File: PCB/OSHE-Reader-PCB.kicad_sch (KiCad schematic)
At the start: 1 part

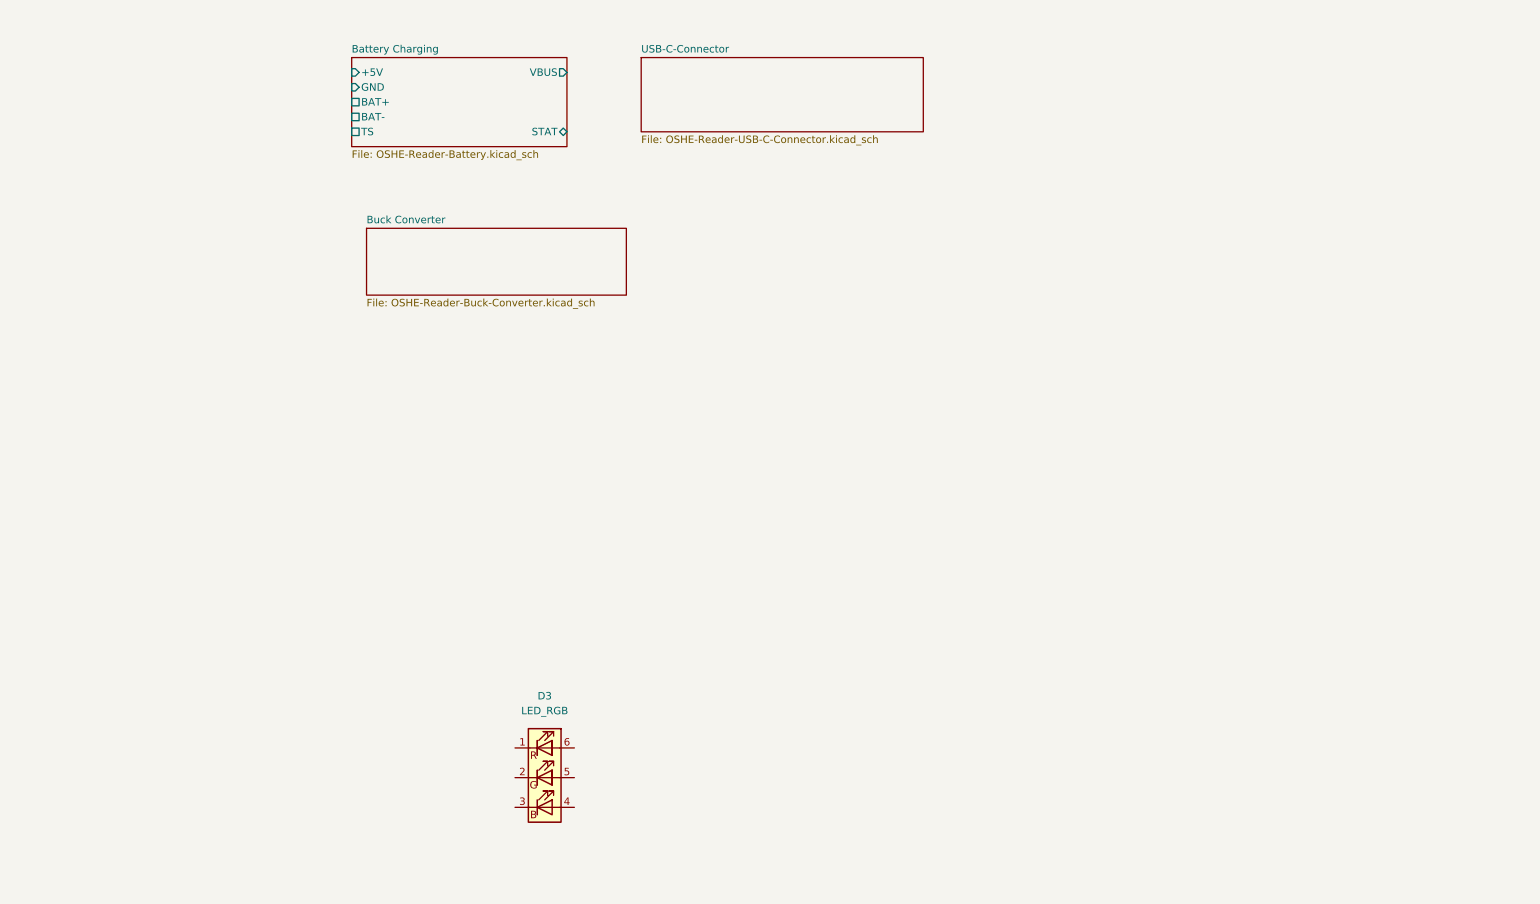
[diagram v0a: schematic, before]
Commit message: added hierarchical symbols to Buck, and did miscelaneous fixes
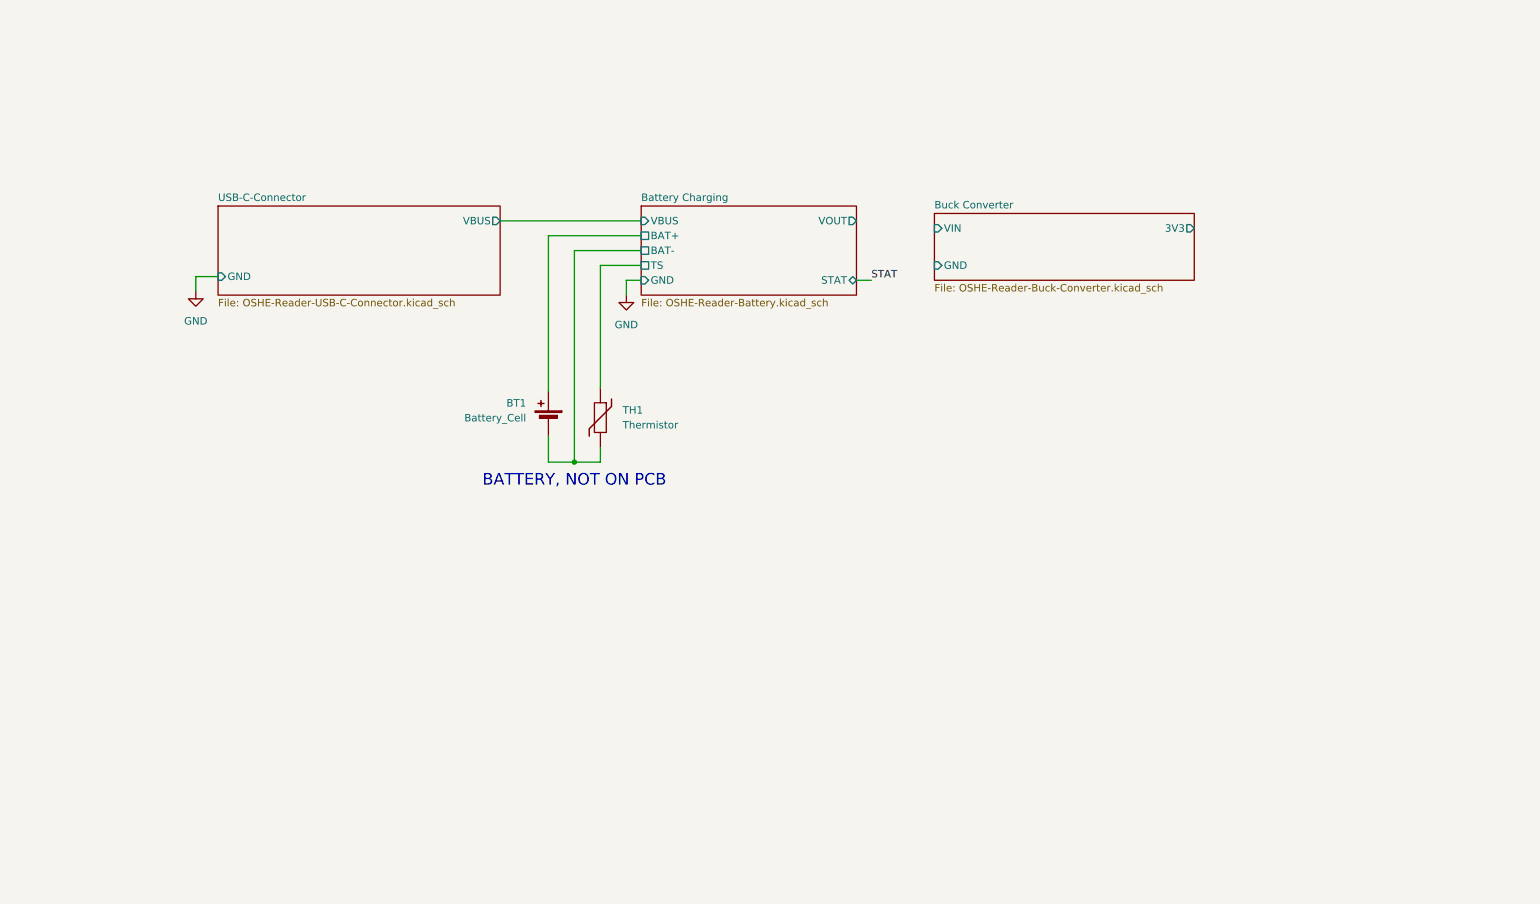
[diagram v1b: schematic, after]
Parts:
- removed D3: LED_RGB, symbol Device:LED_RGB
- added BT1: Battery_Cell, symbol Device:Battery_Cell
- added TH1: Thermistor, symbol Device:Thermistor
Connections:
- net Battery Charging/BAT+: now also BT1.1 (+)
- net Battery Charging/BAT-: now also BT1.2 (-), TH1.2
- net Battery Charging/TS: now also TH1.1
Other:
- sheet Battery Charging ports: added VOUT; removed +5V
- sheet Buck Converter ports: added 3V3, GND, VIN; removed none
- sheet USB-C-Connector ports: added GND, VBUS; removed none
- note added: "BATTERY, NOT ON PCB"

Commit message: fixed up the pcb so everything is *basically* passing ERC
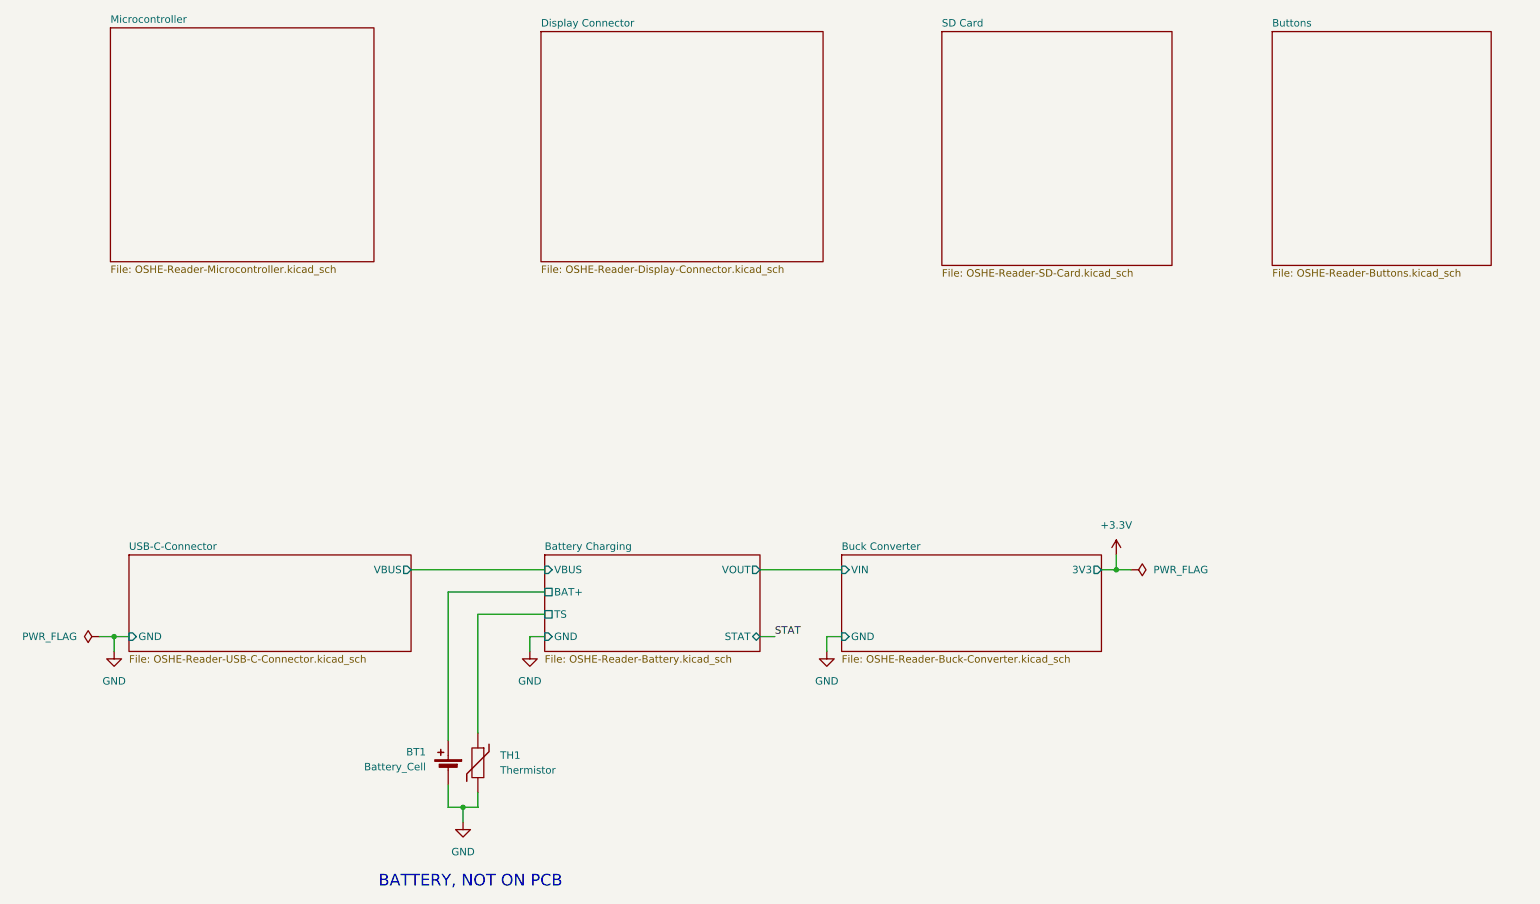
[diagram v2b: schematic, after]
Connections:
- net Battery Charging/BAT- is gone; now on net GND: BT1.2 (-), TH1.2
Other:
- added sheet Buttons (OSHE-Reader-Buttons.kicad_sch)
- added sheet Display Connector (OSHE-Reader-Display-Connector.kicad_sch)
- added sheet Microcontroller (OSHE-Reader-Microcontroller.kicad_sch)
- added sheet SD Card (OSHE-Reader-SD-Card.kicad_sch)
- sheet Battery Charging ports: added none; removed BAT-
- moved on the sheet: BT1, TH1

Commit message: started work adding hierarchical power pins to mcu and sd card sheets
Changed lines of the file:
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@@
 	)
 	(junction
-		(at 201.93 125.73)
+		(at 204.47 125.73)
 		(diameter 0)
 		(color 0 0 0 0)
@@
 	(wire
 		(pts
-			(xy 201.93 123.19) (xy 201.93 125.73)
+			(xy 204.47 123.19) (xy 204.47 125.73)
+		)
+		(stroke
+			(width 0)
+			(type default)
+		)
+	)
+	(wire
+		(pts
+			(xy 204.47 125.73) (xy 207.01 125.73)
+		)
+		(stroke
+			(width 0)
+			(type default)
+		)
+	)
+	(wire
+		(pts
+			(xy 140.97 125.73) (xy 157.48 125.73)
+		)
+		(stroke
+			(width 0)
+			(type default)
+		)
+	)
+	(wire
+		(pts
+			(xy 87.63 166.37) (xy 87.63 162.56)
+		)
+		(stroke
+			(width 0)
+			(type default)
+		)
+	)
+	(wire
+		(pts
+			(xy 90.17 166.37) (xy 90.17 168.91)
+		)
+		(stroke
+			(width 0)
+			(type default)
+		)
+	)
+	(wire
+		(pts
+			(xy 87.63 154.94) (xy 87.63 129.54)
+		)
+		(stroke
+			(width 0)
+			(type default)
+		)
+	)
+	(wire
+		(pts
+			(xy 30.48 137.16) (xy 33.02 137.16)
+		)
+		(stroke
+			(width 0)
+			(type default)
+		)
+	)
+	(wire
+		(pts
+			(xy 30.48 137.16) (xy 30.48 139.7)
+		)
+		(stroke
+			(width 0)
+			(type default)
+		)
+	)
+	(wire
+		(pts
+			(xy 81.28 125.73) (xy 104.14 125.73)
+		)
+		(stroke
+			(width 0)
+			(type default)
+		)
+	)
+	(wire
+		(pts
+			(xy 92.71 133.35) (xy 104.14 133.35)
+		)
+		(stroke
+			(width 0)
+			(type default)
+		)
+	)
+	(wire
+		(pts
+			(xy 90.17 166.37) (xy 92.71 166.37)
 		)
 		(stroke
@@
 	(wire
 		(pts
-			(xy 140.97 125.73) (xy 154.94 125.73)
-		)
-		(stroke
-			(width 0)
-			(type default)
-		)
-	)
-	(wire
-		(pts
-			(xy 87.63 166.37) (xy 87.63 162.56)
-		)
-		(stroke
-			(width 0)
-			(type default)
-		)
-	)
-	(wire
-		(pts
-			(xy 90.17 166.37) (xy 90.17 168.91)
-		)
-		(stroke
-			(width 0)
-			(type default)
-		)
-	)
-	(wire
-		(pts
-			(xy 87.63 154.94) (xy 87.63 129.54)
-		)
-		(stroke
-			(width 0)
-			(type default)
-		)
-	)
-	(wire
-		(pts
-			(xy 30.48 137.16) (xy 33.02 137.16)
-		)
-		(stroke
-			(width 0)
-			(type default)
-		)
-	)
-	(wire
-		(pts
-			(xy 30.48 137.16) (xy 30.48 139.7)
-		)
-		(stroke
-			(width 0)
-			(type default)
-		)
-	)
-	(wire
-		(pts
-			(xy 81.28 125.73) (xy 104.14 125.73)
-		)
-		(stroke
-			(width 0)
-			(type default)
-		)
-	)
-	(wire
-		(pts
-			(xy 92.71 133.35) (xy 104.14 133.35)
-		)
-		(stroke
-			(width 0)
-			(type default)
-		)
-	)
-	(wire
-		(pts
-			(xy 90.17 166.37) (xy 92.71 166.37)
-		)
-		(stroke
-			(width 0)
-			(type default)
-		)
-	)
-	(wire
-		(pts
-			(xy 199.39 125.73) (xy 201.93 125.73)
-		)
-		(stroke
-			(width 0)
-			(type default)
-		)
-	)
-	(wire
-		(pts
 			(xy 92.71 153.67) (xy 92.71 133.35)
 		)
@@
 	(wire
 		(pts
-			(xy 152.4 137.16) (xy 152.4 139.7)
+			(xy 154.94 137.16) (xy 154.94 139.7)
 		)
 		(stroke
@@
 	(wire
 		(pts
-			(xy 152.4 137.16) (xy 154.94 137.16)
-		)
-		(stroke
-			(width 0)
-			(type default)
-		)
-	)
-	(label "STAT"
+			(xy 154.94 137.16) (xy 157.48 137.16)
+		)
+		(stroke
+			(width 0)
+			(type default)
+		)
+	)
+	(label "BAT_STAT"
 		(at 143.51 137.16 0)
 		(effects
@@
 	(symbol
 		(lib_id "power:GND")
-		(at 152.4 139.7 0)
+		(at 154.94 139.7 0)
 		(unit 1)
 		(exclude_from_sim no)
@@
 		(fields_autoplaced yes)
 		(property "Reference" "#PWR03"
-			(at 152.4 146.05 0)
+			(at 154.94 146.05 0)
 			(effects
 				(font
@@
 		)
 		(property "Value" "GND"
-			(at 152.4 144.78 0)
+			(at 154.94 144.78 0)
 			(effects
 				(font
@@
 		)
 		(property "Footprint" ""
-			(at 152.4 139.7 0)
+			(at 154.94 139.7 0)
 			(effects
 				(font
@@
 		)
 		(property "Datasheet" ""
-			(at 152.4 139.7 0)
+			(at 154.94 139.7 0)
 			(effects
 				(font
@@
 		)
 		(property "Description" "Power symbol creates a global label with name \"GND\" , ground"
-			(at 152.4 139.7 0)
+			(at 154.94 139.7 0)
 			(effects
 				(font
@@
 	(symbol
 		(lib_id "power:PWR_FLAG")
-		(at 204.47 125.73 270)
+		(at 207.01 125.73 270)
 		(unit 1)
 		(exclude_from_sim no)
@@
 		(fields_autoplaced yes)
 		(property "Reference" "#FLG02"
-			(at 206.375 125.73 0)
+			(at 208.915 125.73 0)
 			(effects
 				(font
@@
 		)
 		(property "Value" "PWR_FLAG"
-			(at 208.28 125.7299 90)
+			(at 210.82 125.7299 90)
 			(effects
 				(font
@@
 		)
 		(property "Footprint" ""
-			(at 204.47 125.73 0)
+			(at 207.01 125.73 0)
 			(effects
 				(font
@@
 		)
 		(property "Datasheet" "~"
-			(at 204.47 125.73 0)
+			(at 207.01 125.73 0)
 			(effects
 				(font
@@
 		)
 		(property "Description" "Special symbol for telling ERC where power comes from"
-			(at 204.47 125.73 0)
+			(at 207.01 125.73 0)
 			(effects
 				(font
@@
 	(symbol
 		(lib_id "power:+3.3V")
-		(at 201.93 123.19 0)
+		(at 204.47 123.19 0)
 		(unit 1)
 		(exclude_from_sim no)
@@
 		(fields_autoplaced yes)
 		(property "Reference" "#PWR04"
-			(at 201.93 127 0)
+			(at 204.47 127 0)
 			(effects
 				(font
@@
 		)
 		(property "Value" "+3.3V"
-			(at 201.93 118.11 0)
+			(at 204.47 118.11 0)
 			(effects
 				(font
@@
 		)
 		(property "Footprint" ""
-			(at 201.93 123.19 0)
+			(at 204.47 123.19 0)
 			(effects
 				(font
@@
 		)
 		(property "Datasheet" ""
-			(at 201.93 123.19 0)
+			(at 204.47 123.19 0)
 			(effects
 				(font
@@
 		)
 		(property "Description" "Power symbol creates a global label with name \"+3.3V\""
-			(at 201.93 123.19 0)
+			(at 204.47 123.19 0)
 			(effects
 				(font
@@
 	)
 	(sheet
-		(at 154.94 123.19)
+		(at 157.48 123.19)
 		(size 44.45 16.51)
 		(exclude_from_sim no)
@@
 		)
 		(property "Sheetname" "Buck Converter"
-			(at 154.94 122.4784 0)
+			(at 157.48 122.4784 0)
 			(effects
 				(font
@@
 		)
 		(property "Sheetfile" "OSHE-Reader-Buck-Converter.kicad_sch"
-			(at 154.94 140.2846 0)
+			(at 157.48 140.2846 0)
 			(effects
 				(font
@@
 		)
 		(pin "GND" input
-			(at 154.94 137.16 180)
+			(at 157.48 137.16 180)
 			(effects
 				(font
@@
 		)
 		(pin "VIN" input
-			(at 154.94 125.73 180)
+			(at 157.48 125.73 180)
 			(effects
 				(font
@@
 		)
 		(pin "3V3" output
-			(at 199.39 125.73 0)
-			(effects
-				(font
+			(at 201.93 125.73 0)
+			(effects
+				(font

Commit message: Update OSHE-Reader-PCB.kicad_sch
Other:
- sheet Buttons ports: added DownScreenbutton, HomeButton, UpScreenbutton, buttonDownLeft, buttonDownRight, buttonUpLeft, buttonUpRight, centerButton; removed none
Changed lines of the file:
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@@
+			)
+		)
+		(pin "buttonDownLeft" input
+			(at 228.6 39.37 180)
+			(effects
+				(font
+					(size 1.27 1.27)
+				)
+				(justify left)
+			)
+		)
+		(pin "buttonUpLeft" input
+			(at 228.6 48.26 180)
+			(effects
+				(font
+					(size 1.27 1.27)
+				)
+				(justify left)
+			)
+		)
+		(pin "centerButton" input
+			(at 228.6 58.42 180)
+			(effects
+				(font
+					(size 1.27 1.27)
+				)
+				(justify left)
+			)
+		)
+		(pin "buttonDownRight" input
+			(at 228.6 43.18 180)
+			(effects
+				(font
+					(size 1.27 1.27)
+				)
+				(justify left)
+			)
+		)
+		(pin "buttonUpRight" input
+			(at 228.6 52.07 180)
+			(effects
+				(font
+					(size 1.27 1.27)
+				)
+				(justify left)
+			)
+		)
+		(pin "DownScreenbutton" output
+			(at 266.065 40.64 0)
+			(effects
+				(font
+					(size 1.27 1.27)
+				)
+				(justify right)
+			)
+		)
+		(pin "HomeButton" output
+			(at 266.065 58.42 0)
+			(effects
+				(font
+					(size 1.27 1.27)
+				)
+				(justify right)
+			)
+		)
+		(pin "UpScreenbutton" output
+			(at 266.065 49.53 0)
+			(effects
+				(font
+					(size 1.27 1.27)
+				)
+				(justify right)
 			)
 		)

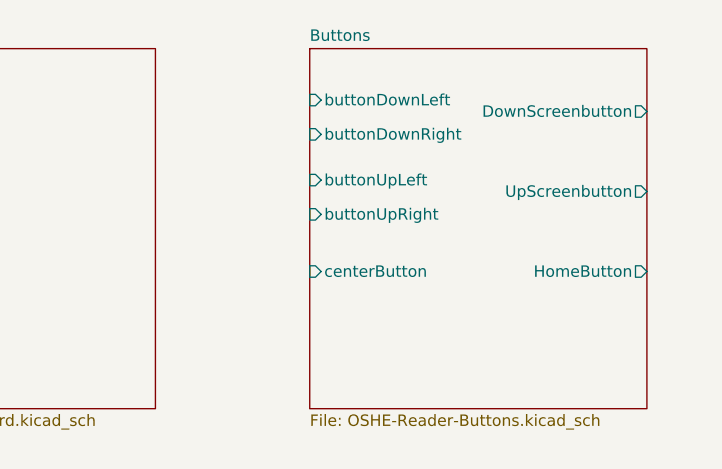
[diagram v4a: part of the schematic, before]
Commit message: oops forgot to update sheet pins
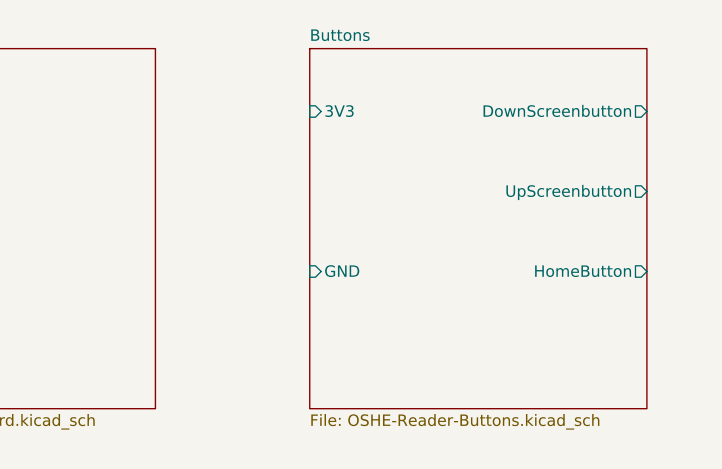
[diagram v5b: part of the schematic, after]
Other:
- sheet Buttons ports: added 3V3, GND; removed buttonDownLeft, buttonDownRight, buttonUpLeft, buttonUpRight, centerButton
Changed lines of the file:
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@@
-			)
-		)
-		(pin "buttonDownLeft" input
-			(at 228.6 39.37 180)
-			(effects
-				(font
-					(size 1.27 1.27)
-				)
-				(justify left)
-			)
-		)
-		(pin "buttonUpLeft" input
-			(at 228.6 48.26 180)
-			(effects
-				(font
-					(size 1.27 1.27)
-				)
-				(justify left)
-			)
-		)
-		(pin "centerButton" input
-			(at 228.6 58.42 180)
-			(effects
-				(font
-					(size 1.27 1.27)
-				)
-				(justify left)
-			)
-		)
-		(pin "buttonDownRight" input
-			(at 228.6 43.18 180)
-			(effects
-				(font
-					(size 1.27 1.27)
-				)
-				(justify left)
-			)
-		)
-		(pin "buttonUpRight" input
-			(at 228.6 52.07 180)
-			(effects
-				(font
-					(size 1.27 1.27)
-				)
-				(justify left)
 			)
 		)
@@
 			)
 		)
+		(pin "GND" input
+			(at 228.6 58.42 180)
+			(effects
+				(font
+					(size 1.27 1.27)
+				)
+				(justify left)
+			)
+		)
+		(pin "3V3" input
+			(at 228.6 40.64 180)
+			(effects
+				(font
+					(size 1.27 1.27)
+				)
+				(justify left)
+			)
+		)

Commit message: hopefully finshed buttons?
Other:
- sheet Buttons ports: added LeftScreenbutton, RightScreenbutton; removed none
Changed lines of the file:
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@@
 		)
 		(pin "HomeButton" output
-			(at 266.065 58.42 0)
+			(at 266.065 52.07 0)
 			(effects
 				(font
@@
 		)
 		(pin "UpScreenbutton" output
-			(at 266.065 49.53 0)
+			(at 266.065 37.465 0)
 			(effects
 				(font
@@
 			)
 		)
+		(pin "LeftScreenbutton" output
+			(at 266.065 44.45 0)
+			(effects
+				(font
+					(size 1.27 1.27)
+				)
+				(justify right)
+			)
+		)
+		(pin "RightScreenbutton" output
+			(at 266.065 48.26 0)
+			(effects
+				(font
+					(size 1.27 1.27)
+				)
+				(justify right)
+			)
+		)

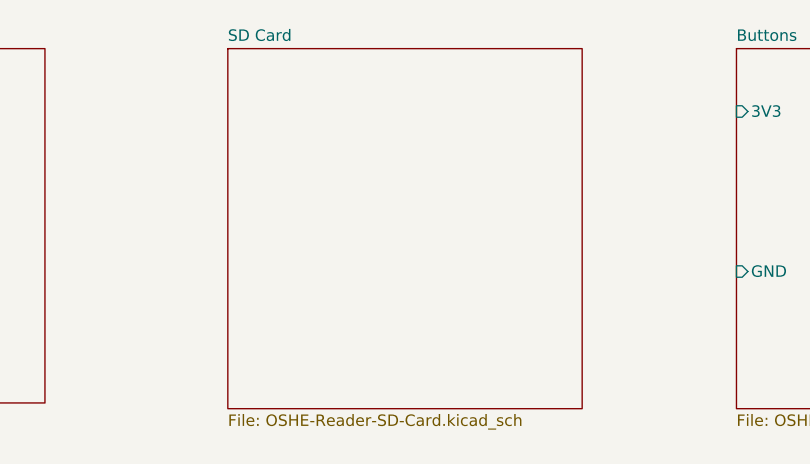
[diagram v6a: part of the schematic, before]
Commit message: sheet pins for SD card module
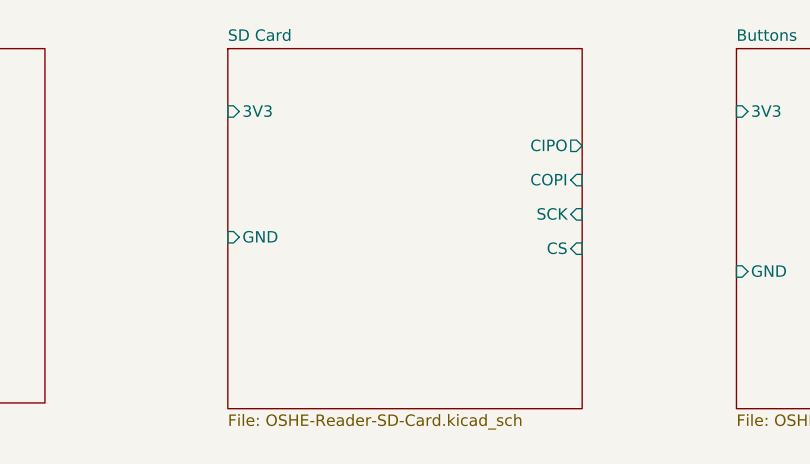
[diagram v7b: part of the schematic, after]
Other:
- sheet SD Card ports: added 3V3, CIPO, COPI, CS, GND, SCK; removed none
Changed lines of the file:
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@@
+			)
+		)
+		(pin "3V3" input
+			(at 172.085 40.64 180)
+			(effects
+				(font
+					(size 1.27 1.27)
+				)
+				(justify left)
+			)
+		)
+		(pin "CS" input
+			(at 211.455 55.88 0)
+			(effects
+				(font
+					(size 1.27 1.27)
+				)
+				(justify right)
+			)
+		)
+		(pin "GND" input
+			(at 172.085 54.61 180)
+			(effects
+				(font
+					(size 1.27 1.27)
+				)
+				(justify left)
+			)
+		)
+		(pin "CIPO" output
+			(at 211.455 44.45 0)
+			(effects
+				(font
+					(size 1.27 1.27)
+				)
+				(justify right)
+			)
+		)
+		(pin "COPI" input
+			(at 211.455 48.26 0)
+			(effects
+				(font
+					(size 1.27 1.27)
+				)
+				(justify right)
+			)
+		)
+		(pin "SCK" input
+			(at 211.455 52.07 0)
+			(effects
+				(font
+					(size 1.27 1.27)
+				)
+				(justify right)
 			)
 		)
